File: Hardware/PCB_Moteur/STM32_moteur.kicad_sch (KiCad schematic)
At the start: 55 parts, among them J2 Conn_01x06_Pin, U1 STM32F103CBT6

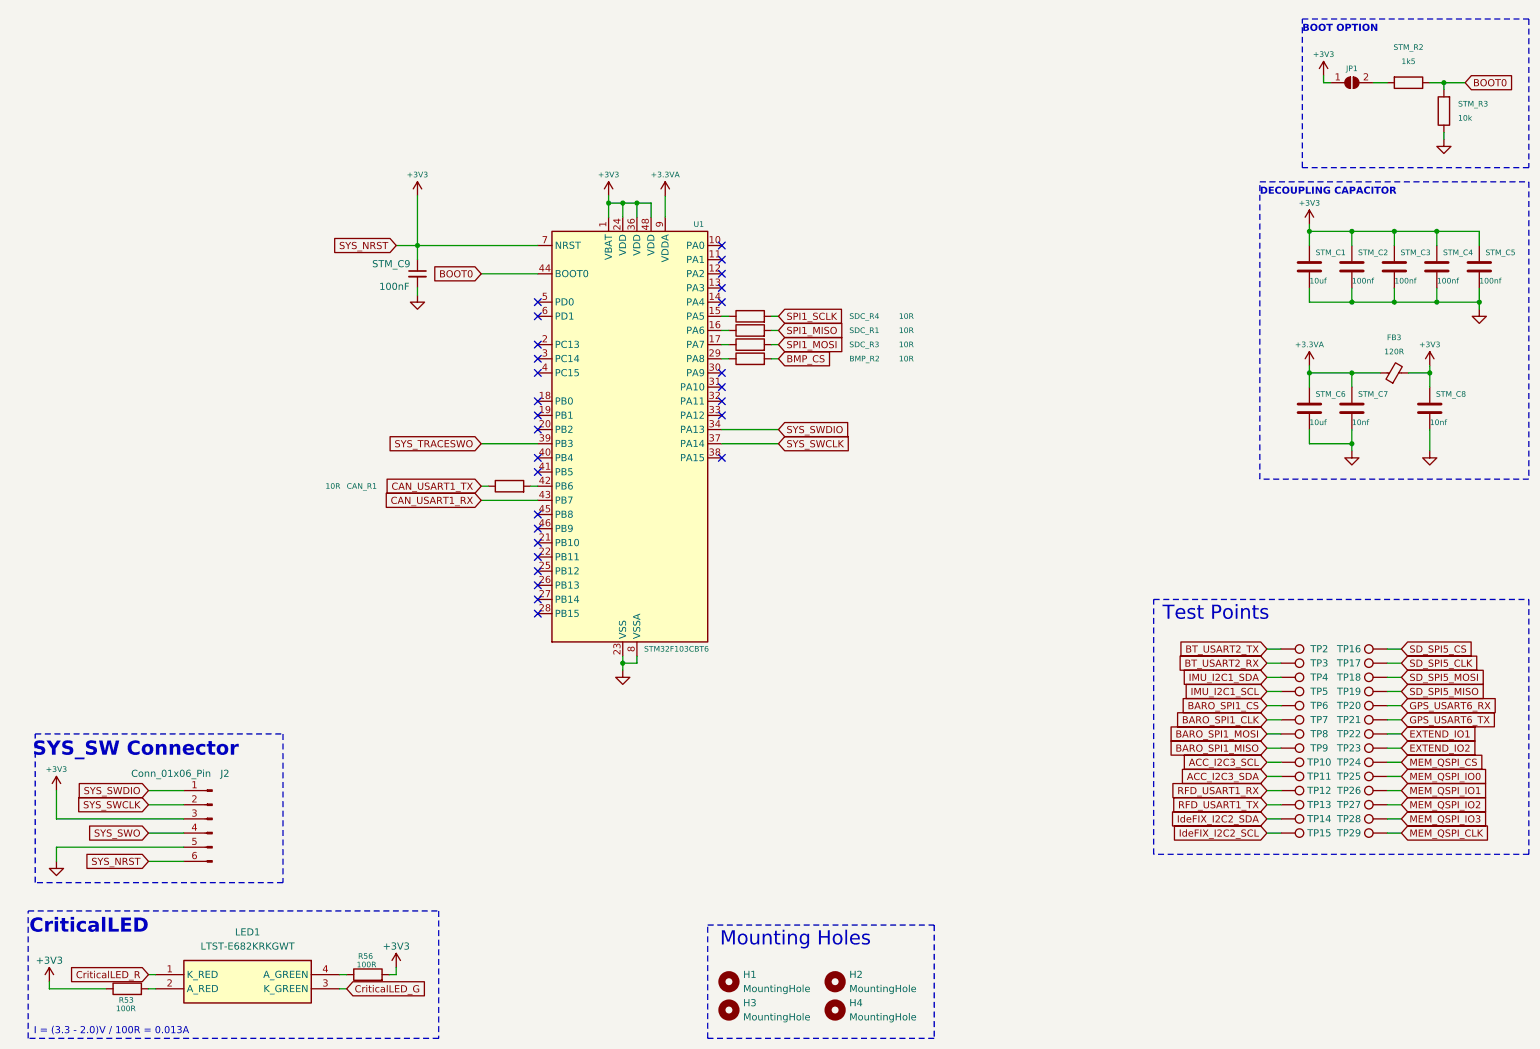
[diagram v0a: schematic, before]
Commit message: feat: setup stm32 project + mapping + add led LDO
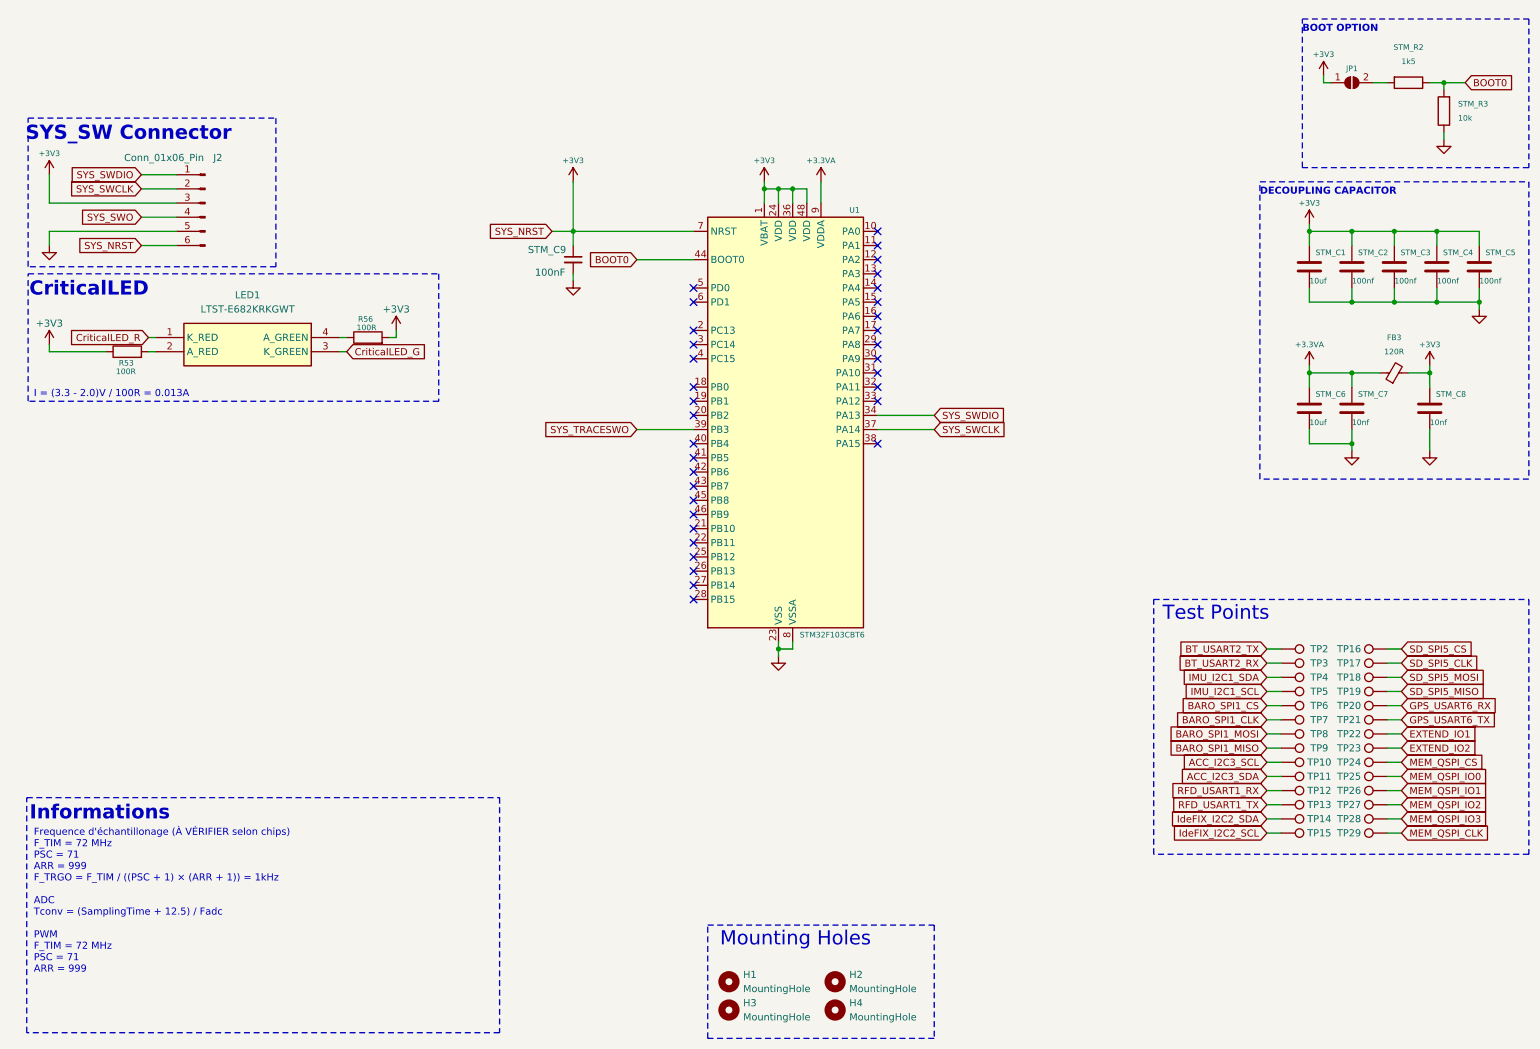
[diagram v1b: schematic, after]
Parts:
- removed BMP_R2, CAN_R1, SDC_R1, SDC_R3, SDC_R4: 10R, Resistor_SMD:R_0805_2012Metric, symbol Device:R
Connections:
- net CAN_USART1_RX: no longer names the net of U1.43 (PB7)
- no-connect marks 28 -> 34
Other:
- note added: "Frequence d'échantillonage (À VÉRIFIER selon chips) F_TIM = 72 MHz PSC = 71 ARR = 999 F_TRGO = F_TIM / ((PSC + 1) × (ARR + 1)) = 1kHz ADC Tconv = (SamplingTime + 12.5) / Fadc PWM F_TIM = 72 MHz PSC = 71 ARR = 999"
- note added: "Informations"
- moved on the sheet: J2, LED1, R53, R56, STM_C9, U1

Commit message: wip : pin mapping on STM32 and limit switch circuit
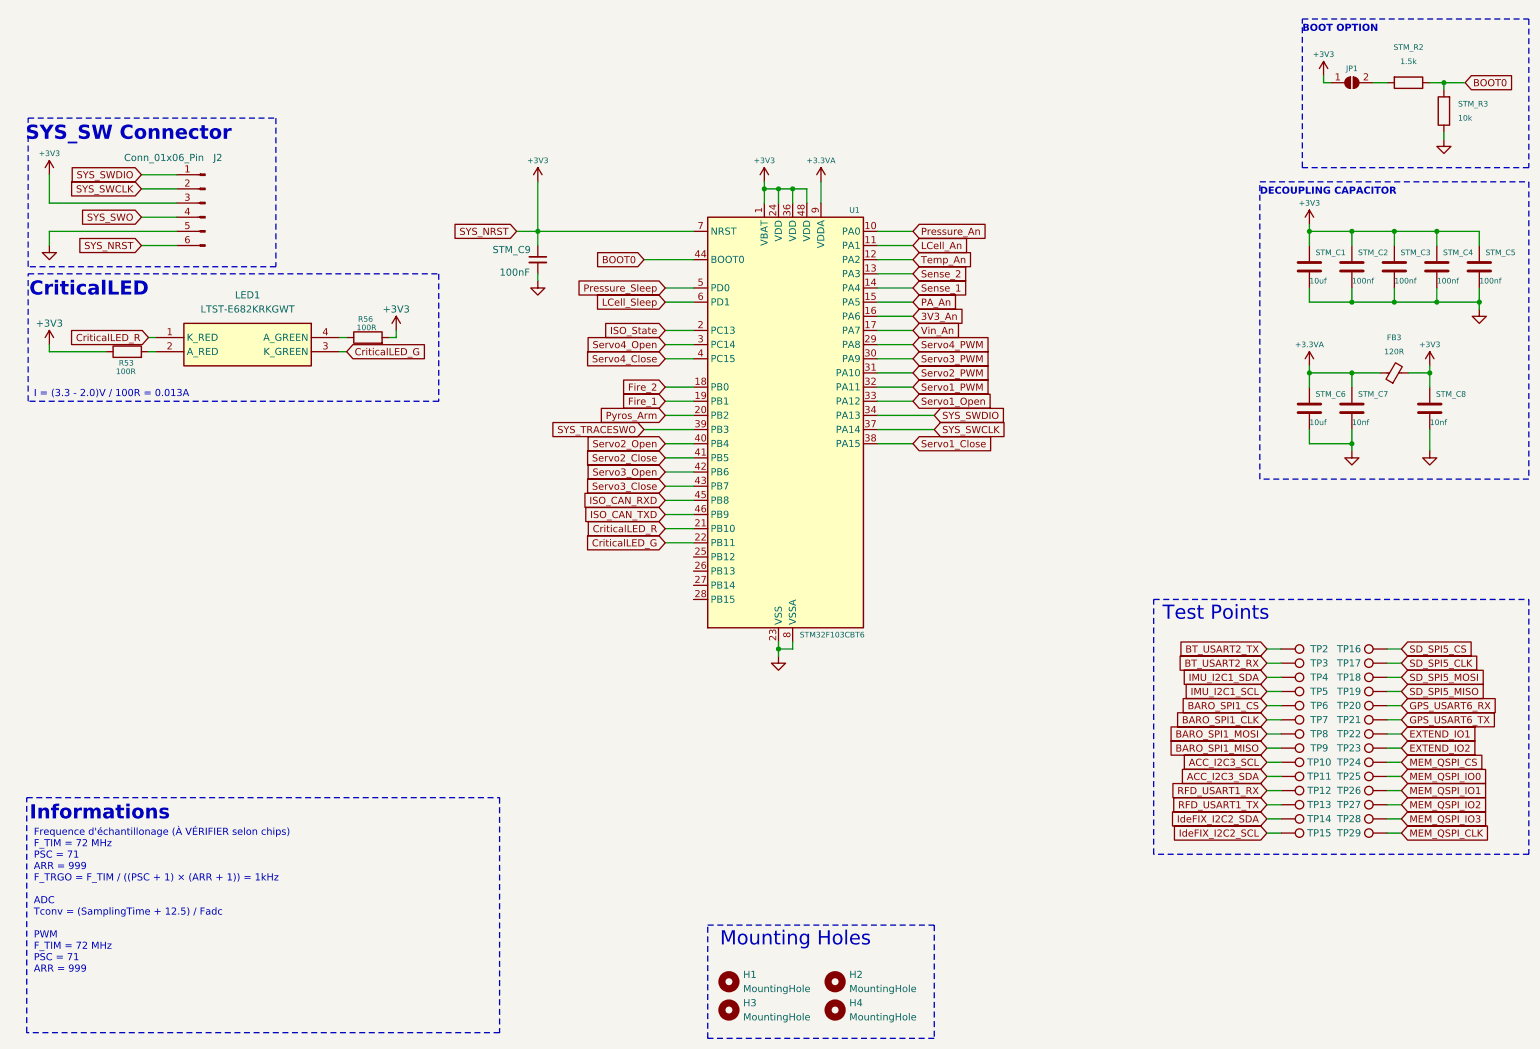
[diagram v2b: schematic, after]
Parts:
- STM_R2: value 1k5 -> 1.5k
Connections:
- net CriticalLED_G: now also U1.22 (PB11)
- net CriticalLED_R: now also U1.21 (PB10)
- net Pressure_An: now reaches U1.10 (PA0)
- net LCell_An: now reaches U1.11 (PA1)
- net Temp_An: now reaches U1.12 (PA2)
- net Sense_2: now reaches U1.13 (PA3)
- net Sense_1: now reaches U1.14 (PA4)
- net PA_An: now reaches U1.15 (PA5)
- net 3V3_An: now reaches U1.16 (PA6)
- net Vin_An: now reaches U1.17 (PA7)
- net Fire_2: now reaches U1.18 (PB0)
- net Fire_1: now reaches U1.19 (PB1)
- net ISO_State: now reaches U1.2 (PC13)
- net Pyros_Arm: now reaches U1.20 (PB2)
- net Servo4_PWM: now reaches U1.29 (PA8)
- net Servo4_Open: now reaches U1.3 (PC14)
- net Servo3_PWM: now reaches U1.30 (PA9)
- net Servo2_PWM: now reaches U1.31 (PA10)
- net Servo1_PWM: now reaches U1.32 (PA11)
- net Servo1_Open: now reaches U1.33 (PA12)
- net Servo1_Close: now reaches U1.38 (PA15)
- net Servo4_Close: now reaches U1.4 (PC15)
- net Servo2_Open: now reaches U1.40 (PB4)
- net Servo2_Close: now reaches U1.41 (PB5)
- net Servo3_Open: now reaches U1.42 (PB6)
- net Servo3_Close: now reaches U1.43 (PB7)
- net ISO_CAN_RXD: now reaches U1.45 (PB8)
- net ISO_CAN_TXD: now reaches U1.46 (PB9)
- net Pressure_Sleep: now reaches U1.5 (PD0)
- net LCell_Sleep: now reaches U1.6 (PD1)
- no-connect marks 34 -> 0
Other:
- moved on the sheet: STM_C9

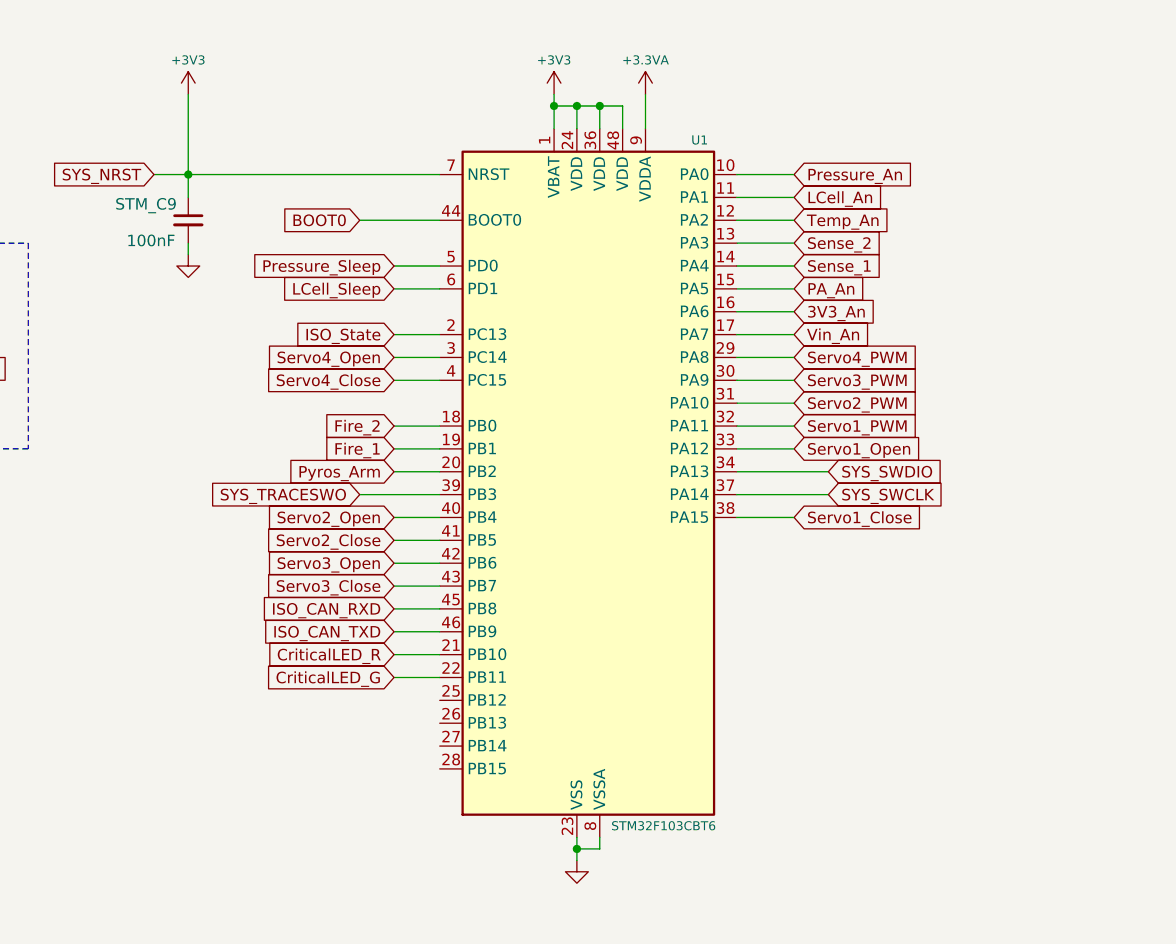
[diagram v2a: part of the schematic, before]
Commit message: feat: add extend ios + fix mapping kicad + add transmitter resistors
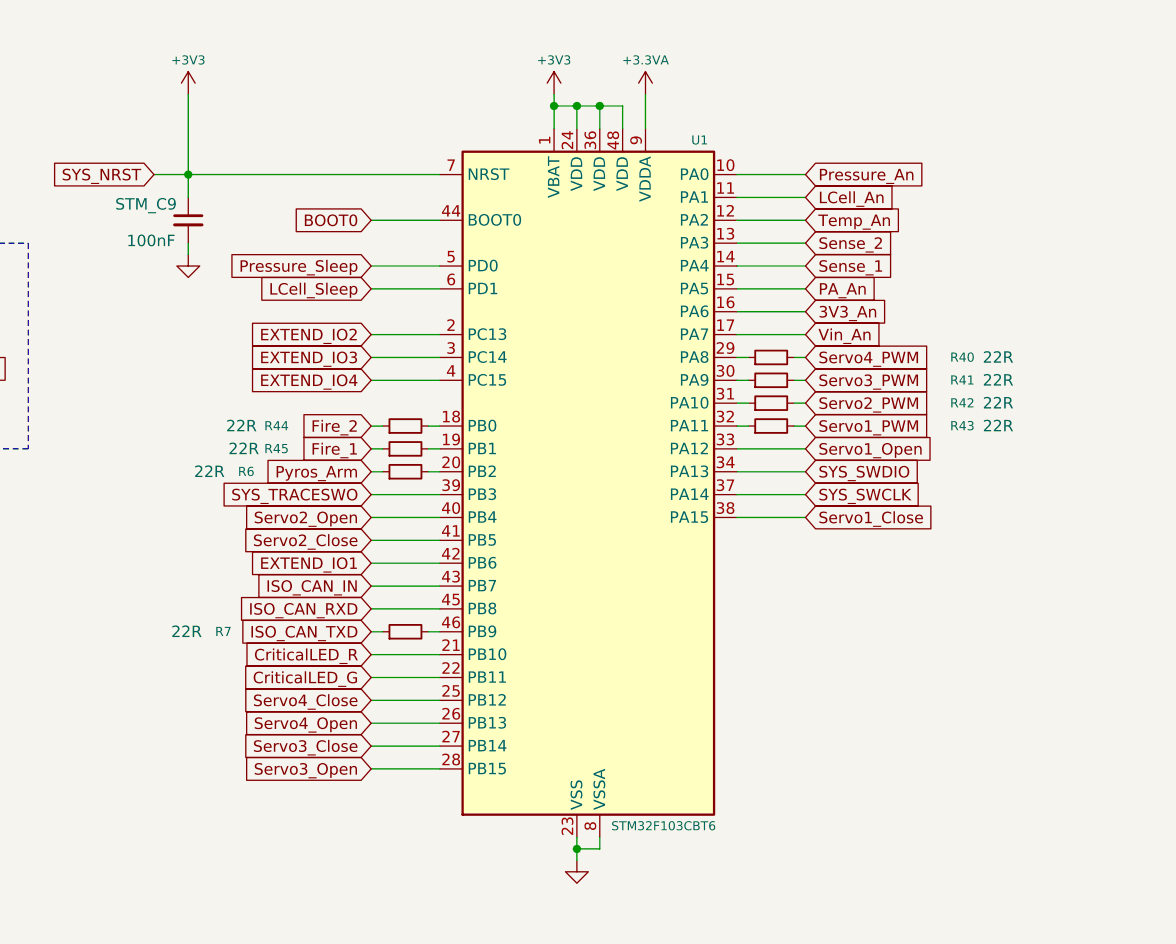
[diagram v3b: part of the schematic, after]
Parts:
- added R40, R41, R42, R43, R44, R45, R6, R7: 22R, Resistor_SMD:R_0603_1608Metric, symbol Device:R_Small
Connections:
- net ISO_State is gone; now on net EXTEND_IO2: U1.2 (PC13)
- net EXTEND_IO1: now also U1.42 (PB6)
- net Fire_1: now also R45.1; no longer U1.19 (PB1)
- net Fire_2: now also R44.1; no longer U1.18 (PB0)
- net ISO_CAN_TXD: now also R7.1; no longer U1.46 (PB9)
- net Pyros_Arm: now also R6.1; no longer U1.20 (PB2)
- net Servo1_PWM: now also R43.2; no longer U1.32 (PA11)
- net Servo2_PWM: now also R42.2; no longer U1.31 (PA10)
- net Servo3_Close: now also U1.27 (PB14); no longer U1.43 (PB7)
- net Servo3_Open: now also U1.28 (PB15); no longer U1.42 (PB6)
- net Servo3_PWM: now also R41.2; no longer U1.30 (PA9)
- net Servo4_Close: now also U1.25 (PB12); no longer U1.4 (PC15)
- net Servo4_Open: now also U1.26 (PB13); no longer U1.3 (PC14)
- net Servo4_PWM: now also R40.2; no longer U1.29 (PA8)
- new net: R41.1, U1.30 (PA9)
- new net: R44.2, U1.18 (PB0)
- new net: R45.2, U1.19 (PB1)
- new net: R6.2, U1.20 (PB2)
- new net: R40.1, U1.29 (PA8)
- new net: R42.1, U1.31 (PA10)
- new net: R43.1, U1.32 (PA11)
- new net: R7.2, U1.46 (PB9)
- new net EXTEND_IO3: U1.3 (PC14)
- new net EXTEND_IO4: U1.4 (PC15)
- new net ISO_CAN_IN: U1.43 (PB7)
